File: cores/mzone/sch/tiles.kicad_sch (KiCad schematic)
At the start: 37 parts

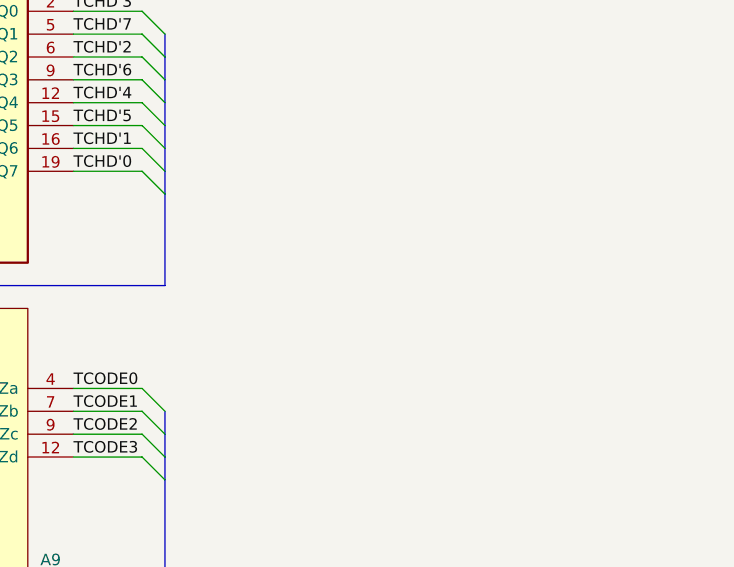
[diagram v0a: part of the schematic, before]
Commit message: mzone core
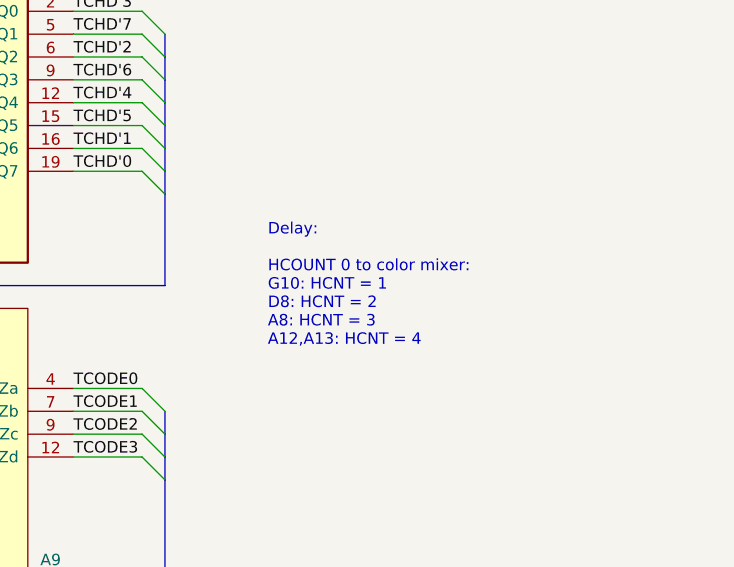
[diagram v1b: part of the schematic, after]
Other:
- note added: "Delay: HCOUNT 0 to color mixer: G10: HCNT = 1 D8: HCNT = 2 A8: HCNT = 3 A12,A13: HCNT = 4"

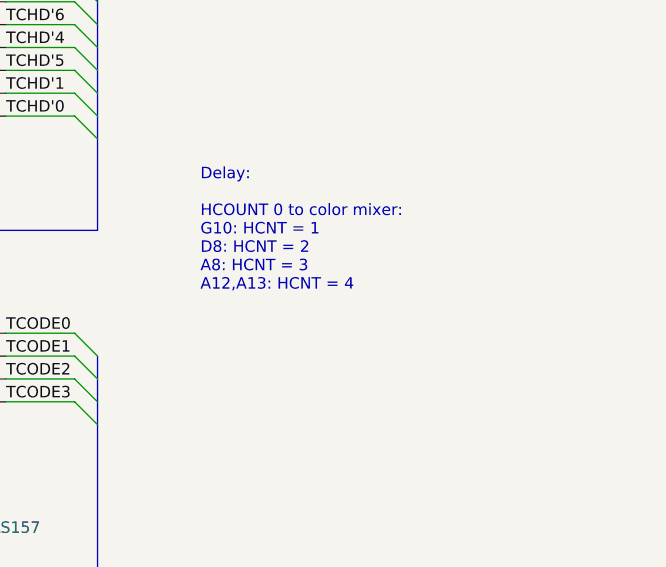
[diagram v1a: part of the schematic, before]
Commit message: mzone core
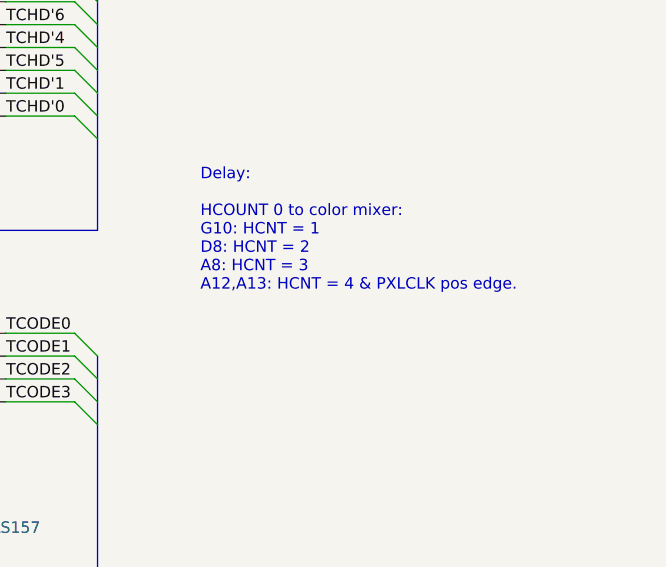
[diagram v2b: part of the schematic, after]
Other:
- note added: "Delay: HCOUNT 0 to color mixer: G10: HCNT = 1 D8: HCNT = 2 A8: HCNT = 3 A12,A13: HCNT = 4 & PXLCLK pos edge."
- note removed: "Delay: HCOUNT 0 to color mixer: G10: HCNT = 1 D8: HCNT = 2 A8: HCNT = 3 A12,A13: HCNT = 4"
